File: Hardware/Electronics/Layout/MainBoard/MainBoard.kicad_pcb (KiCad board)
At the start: 2 copper layers, 91.8 x 91.6 mm, 71 parts, among them P10 AUX, P2 CONN_02X08, P3 SWD/JTAG, P4 BUTTON1, P5 BUTTON2, P6 BUTTON3, P7 BUTTON4, P8 POWER_IN, P9 DEBUG_UART, SW1 STM_RESET, SW2 ESP_RESET, SW3 ESP_PROG, U10 S25FL129P, U11 MAX9700, U12 STM32L452VCTx, U13 LSM9DS1, U14 BME280, U15 TPS6211, U9 ESP-12F, Y1 8MHz, Y2 32.768kHz

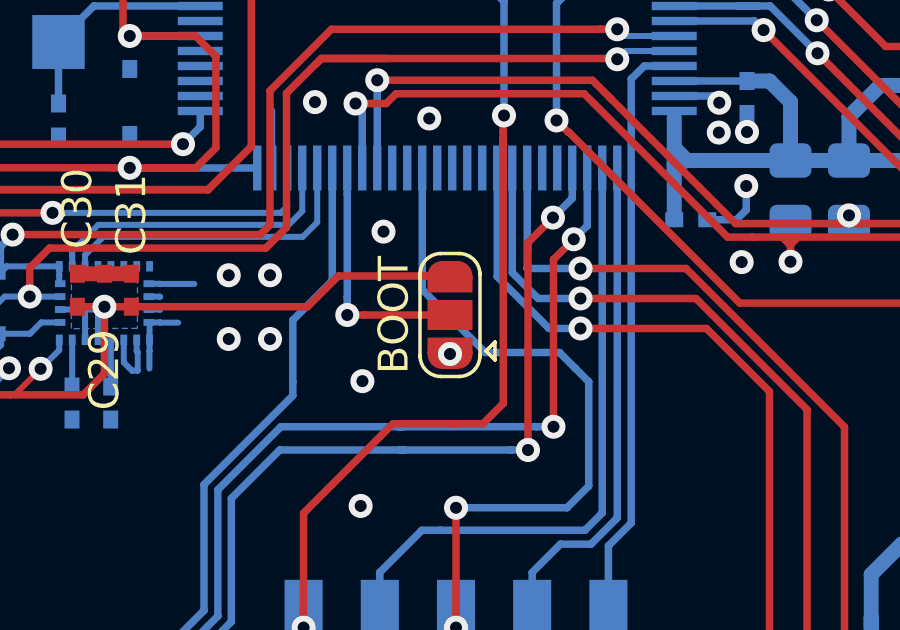
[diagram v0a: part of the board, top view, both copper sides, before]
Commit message: updated schematics
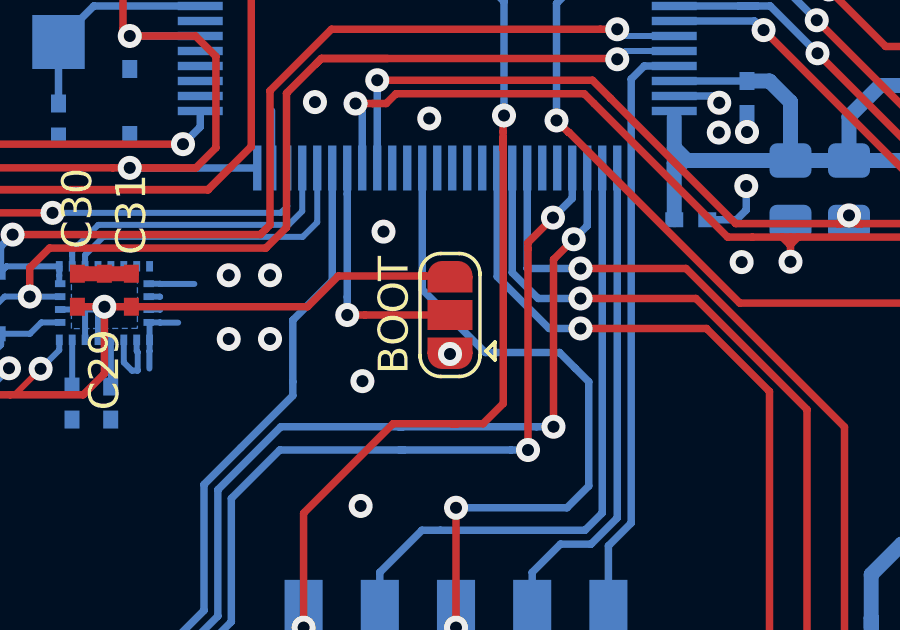
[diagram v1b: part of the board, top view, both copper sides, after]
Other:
- net class Default removed
- net class thin removed
